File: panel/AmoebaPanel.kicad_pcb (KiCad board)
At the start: 2 copper layers, 92 x 84 mm, 168 parts, among them J1 Conn_01x01_Pin, J2 Conn_01x01_Pin, J3 Conn_01x01_Pin, J4 Conn_01x01_Pin, SW1 SW_SPST

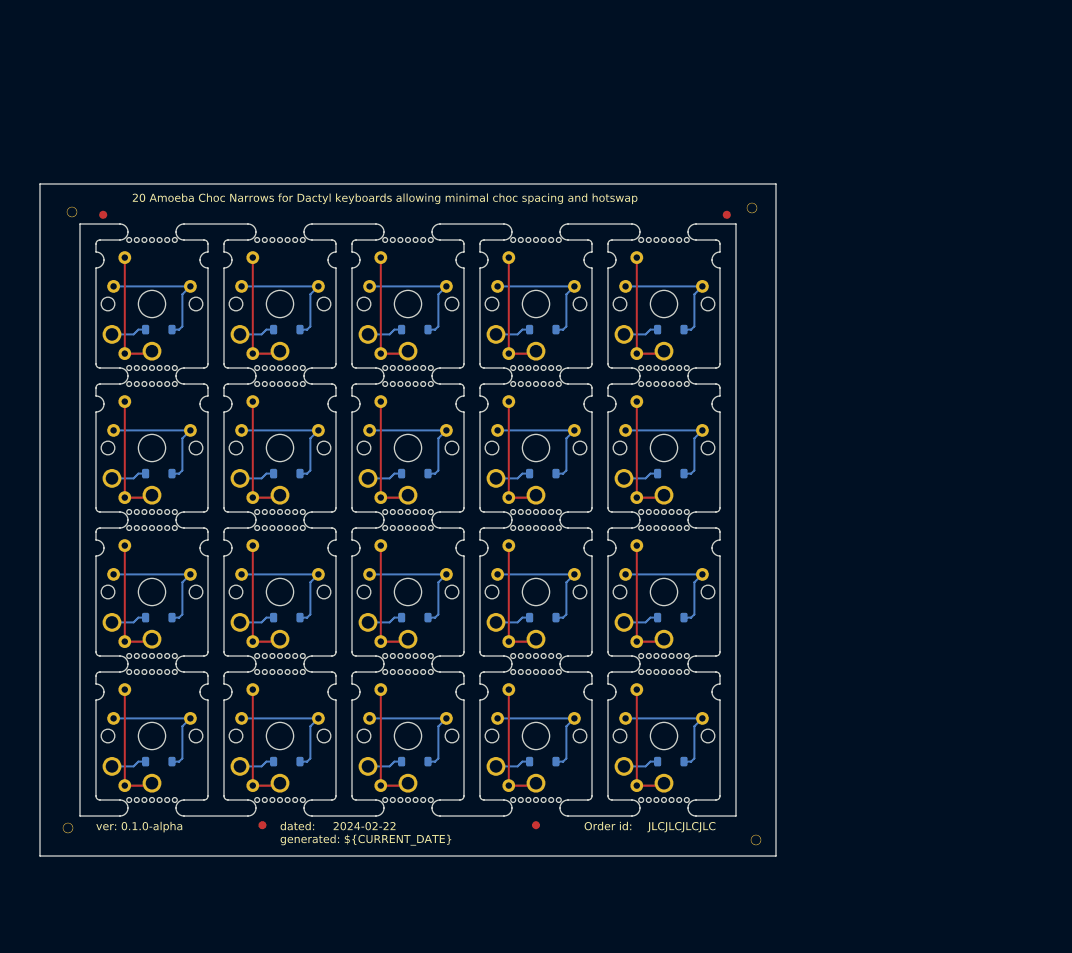
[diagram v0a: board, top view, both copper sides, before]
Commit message: feat(panel): 5 x 5 grid, docs
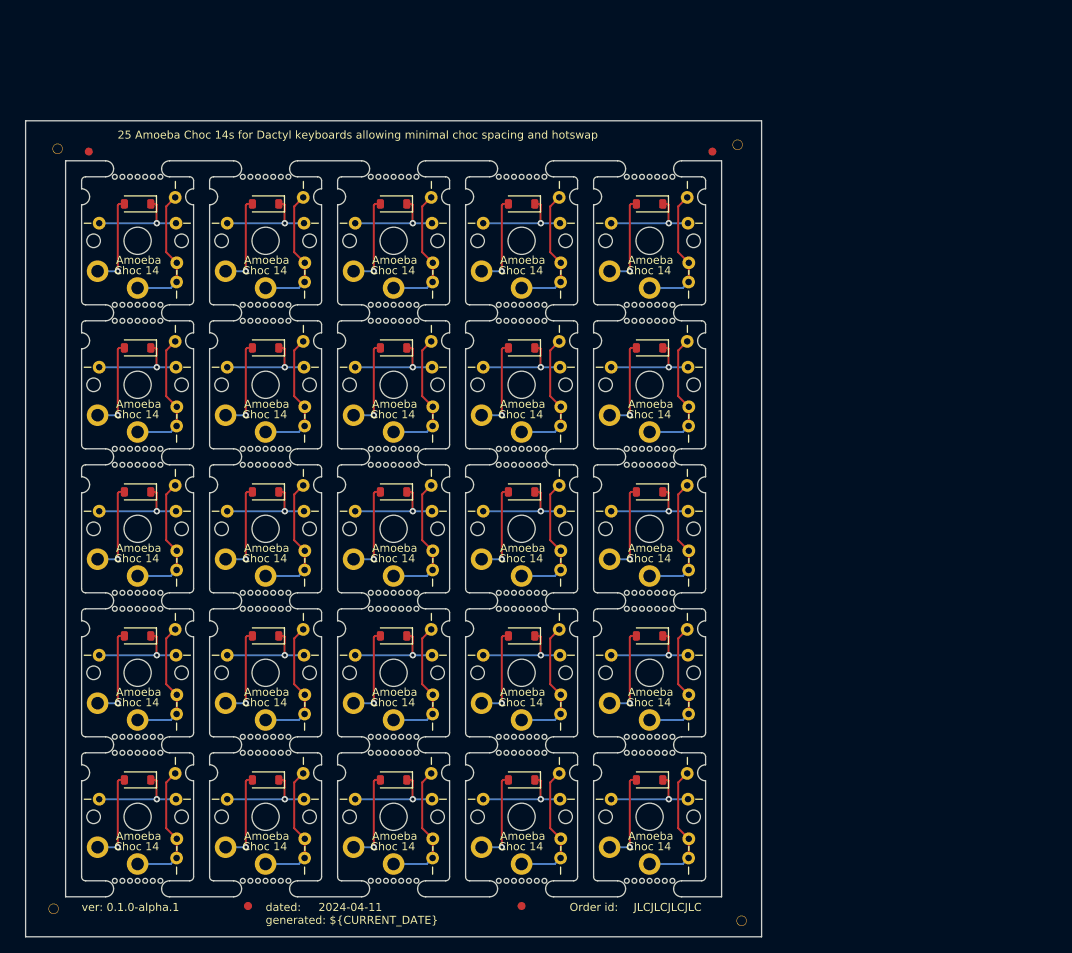
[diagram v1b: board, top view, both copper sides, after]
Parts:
- removed the D1 at (111.8, 107.2)
- removed the D1 at (127.8, 89.2)
- removed the D1 at (175.8, 125.2)
- removed the D1 at (111.8, 89.2)
- removed the D1 at (127.8, 143.2)
- removed the D1 at (127.8, 125.2)
- removed the D1 at (159.8, 107.2)
- removed the D1 at (159.8, 89.2)
- removed the D1 at (111.8, 143.2)
- removed the D1 at (143.8, 89.2)
- removed the D1 at (127.8, 107.2)
- removed the D1 at (143.8, 107.2)
- removed the D1 at (143.8, 143.2)
- removed the D1 at (159.8, 125.2)
- removed the D1 at (175.8, 89.2)
- removed the D1 at (175.8, 143.2)
- removed the D1 at (175.8, 107.2)
- removed the D1 at (111.8, 125.2)
- removed the D1 at (143.8, 125.2)
- removed the D1 at (159.8, 143.2)
- removed the J1 at (107.6, 116.2)
- removed the J1 at (171.6, 134.2)
- removed the J1 at (171.6, 80.2)
- removed the J1 at (139.6, 98.2)
- removed the J1 at (155.6, 134.2)
- removed the J1 at (123.6, 116.2)
- removed the J1 at (107.6, 134.2)
- removed the J1 at (123.6, 134.2)
- removed the J1 at (123.6, 80.2)
- removed the J1 at (171.6, 98.2)
- removed the J1 at (171.6, 116.2)
- removed the J1 at (107.6, 98.2)
- removed the J1 at (123.6, 98.2)
- removed the J1 at (155.6, 98.2)
- removed the J1 at (155.6, 116.2)
- removed the J1 at (139.6, 80.2)
- removed the J1 at (139.6, 116.2)
- removed the J1 at (107.6, 80.2)
- removed the J1 at (139.6, 134.2)
- removed the J1 at (155.6, 80.2)
- removed the J2 at (155.6, 92.2)
- removed the J2 at (123.6, 128.2)
- removed the J2 at (107.6, 128.2)
- removed the J2 at (139.6, 92.2)
- removed the J2 at (139.6, 110.2)
- removed the J2 at (123.6, 110.2)
- removed the J2 at (171.6, 110.2)
- removed the J2 at (107.6, 92.2)
- removed the J2 at (139.6, 128.2)
- removed the J2 at (171.6, 128.2)
- removed the J2 at (155.6, 128.2)
- removed the J2 at (107.6, 146.2)
- removed the J2 at (107.6, 110.2)
- removed the J2 at (123.6, 92.2)
- removed the J2 at (139.6, 146.2)
- removed the J2 at (171.6, 92.2)
- removed the J2 at (155.6, 110.2)
- removed the J2 at (123.6, 146.2)
- removed the J2 at (155.6, 146.2)
- removed the J2 at (171.6, 146.2)
- removed the J3 at (138.2, 119.8)
- removed the J3 at (154.2, 137.8)
- removed the J3 at (106.2, 119.8)
- removed the J3 at (138.2, 101.8)
- removed the J3 at (106.2, 101.8)
- removed the J3 at (106.2, 137.8)
- removed the J3 at (170.2, 83.8)
- removed the J3 at (106.2, 83.8)
- removed the J3 at (154.2, 101.8)
- removed the J3 at (122.2, 83.8)
- removed the J3 at (122.2, 101.8)
- removed the J3 at (154.2, 119.8)
- removed the J3 at (170.2, 101.8)
- removed the J3 at (170.2, 137.8)
- removed the J3 at (138.2, 137.8)
- removed the J3 at (122.2, 137.8)
- removed the J3 at (122.2, 119.8)
- removed the J3 at (138.2, 83.8)
- removed the J3 at (154.2, 83.8)
- removed the J3 at (170.2, 119.8)
- removed the J4 at (131.8, 83.8)
- removed the J4 at (163.8, 119.8)
- removed the J4 at (163.8, 137.8)
- removed the J4 at (131.8, 101.8)
- removed the J4 at (163.8, 83.8)
- removed the J4 at (147.8, 83.8)
- removed the J4 at (147.8, 119.8)
- removed the J4 at (115.8, 83.8)
- removed the J4 at (179.8, 83.8)
- removed the J4 at (179.8, 137.8)
- removed the J4 at (147.8, 137.8)
- removed the J4 at (179.8, 101.8)
- removed the J4 at (115.8, 119.8)
- removed the J4 at (179.8, 119.8)
- removed the J4 at (115.8, 101.8)
- removed the J4 at (131.8, 137.8)
- removed the J4 at (115.8, 137.8)
- removed the J4 at (147.8, 101.8)
- removed the J4 at (131.8, 119.8)
- removed the J4 at (163.8, 101.8)
- removed the REF** at (159.0, 132.0)
- removed the REF** at (175.0, 96.0)
- removed the REF** at (111.0, 114.0)
- removed the REF** at (127.0, 132.0)
- removed the REF** at (175.0, 132.0)
- removed the REF** at (175.0, 112.0)
- removed the REF** at (175.0, 130.0)
- removed the REF** at (175.0, 94.0)
- removed the REF** at (111.0, 96.0)
- removed the REF** at (159.0, 148.0)
- removed the REF** at (127.0, 148.0)
- removed the REF** at (159.0, 78.0)
- removed the REF** at (127.0, 112.0)
- removed the REF** at (143.0, 130.0)
- removed the REF** at (159.0, 96.0)
- removed the REF** at (127.0, 130.0)
- removed the REF** at (111.0, 132.0)
- removed the REF** at (111.0, 78.0)
- removed the REF** at (175.0, 114.0)
- removed the REF** at (143.0, 78.0)
- removed the REF** at (143.0, 94.0)
- removed the REF** at (159.0, 114.0)
- removed the REF** at (127.0, 78.0)
- removed the REF** at (175.0, 78.0)
- removed the REF** at (175.0, 148.0)
- removed the REF** at (143.0, 148.0)
- removed the REF** at (127.0, 94.0)
- removed the REF** at (143.0, 112.0)
- removed the REF** at (111.0, 94.0)
- removed the REF** at (143.0, 114.0)
- removed the REF** at (127.0, 114.0)
- removed the REF** at (143.0, 96.0)
- removed the REF** at (159.0, 112.0)
- removed the REF** at (111.0, 112.0)
- removed the REF** at (159.0, 94.0)
- removed the REF** at (143.0, 132.0)
- removed the REF** at (111.0, 130.0)
- removed the REF** at (111.0, 148.0)
- removed the REF** at (159.0, 130.0)
- removed the REF** at (127.0, 96.0)
- removed the SW1 at (111.0, 122.0)
- removed the SW1 at (159.0, 86.0)
- removed the SW1 at (175.0, 104.0)
- removed the SW1 at (111.0, 86.0)
- removed the SW1 at (111.0, 140.0)
- removed the SW1 at (159.0, 104.0)
- removed the SW1 at (111.0, 104.0)
- removed the SW1 at (175.0, 86.0)
- removed the SW1 at (143.0, 86.0)
- removed the SW1 at (159.0, 140.0)
- removed the SW1 at (143.0, 140.0)
- removed the SW1 at (175.0, 122.0)
- removed the SW1 at (127.0, 122.0)
- removed the SW1 at (127.0, 140.0)
- removed the SW1 at (143.0, 104.0)
- removed the SW1 at (159.0, 122.0)
- removed the SW1 at (127.0, 86.0)
- removed the SW1 at (127.0, 104.0)
- removed the SW1 at (143.0, 122.0)
- removed the SW1 at (175.0, 140.0)
- added D1: 1N4148, Diode_SMD:D_SOD-123, F.Cu at (109.2, 73.5)
- added D10: 1N4148, Diode_SMD:D_SOD-123, F.Cu at (173.2, 91.5)
- added D11: 1N4148, Diode_SMD:D_SOD-123, F.Cu at (109.2, 109.5)
- added D12: 1N4148, Diode_SMD:D_SOD-123, F.Cu at (125.2, 109.5)
- added D13: 1N4148, Diode_SMD:D_SOD-123, F.Cu at (141.2, 109.5)
- added D14: 1N4148, Diode_SMD:D_SOD-123, F.Cu at (157.2, 109.5)
- added D15: 1N4148, Diode_SMD:D_SOD-123, F.Cu at (173.2, 109.5)
- added D16: 1N4148, Diode_SMD:D_SOD-123, F.Cu at (109.2, 127.5)
- added D17: 1N4148, Diode_SMD:D_SOD-123, F.Cu at (125.2, 127.5)
- added D18: 1N4148, Diode_SMD:D_SOD-123, F.Cu at (141.2, 127.5)
- added D19: 1N4148, Diode_SMD:D_SOD-123, F.Cu at (157.2, 127.5)
- added D2: 1N4148, Diode_SMD:D_SOD-123, F.Cu at (125.2, 73.5)
- added D20: 1N4148, Diode_SMD:D_SOD-123, F.Cu at (173.2, 127.5)
- added D21: 1N4148, Diode_SMD:D_SOD-123, F.Cu at (109.2, 145.5)
- added D22: 1N4148, Diode_SMD:D_SOD-123, F.Cu at (125.2, 145.5)
- added D23: 1N4148, Diode_SMD:D_SOD-123, F.Cu at (141.2, 145.5)
- added D24: 1N4148, Diode_SMD:D_SOD-123, F.Cu at (157.2, 145.5)
- added D25: 1N4148, Diode_SMD:D_SOD-123, F.Cu at (173.2, 145.5)
- added D3: 1N4148, Diode_SMD:D_SOD-123, F.Cu at (141.2, 73.5)
- added D4: 1N4148, Diode_SMD:D_SOD-123, F.Cu at (157.2, 73.5)
- added D5: 1N4148, Diode_SMD:D_SOD-123, F.Cu at (173.2, 73.5)
- added D6: 1N4148, Diode_SMD:D_SOD-123, F.Cu at (109.2, 91.5)
- added D7: 1N4148, Diode_SMD:D_SOD-123, F.Cu at (125.2, 91.5)
- added D8: 1N4148, Diode_SMD:D_SOD-123, F.Cu at (141.2, 91.5)
- added D9: 1N4148, Diode_SMD:D_SOD-123, F.Cu at (157.2, 91.5)
- added J1: Conn_01x01_Pin, Amoeba_Choc_Nar:Pin_D0.8mm_L7.0mm, B.Cu at (113.9, 72.7)
- added J10: Conn_01x01_Pin, Amoeba_Choc_Nar:Pin_D0.8mm_L7.0mm, B.Cu at (130.1, 80.8)
- added J100: Conn_01x01_Pin, Amoeba_Choc_Nar:Pin_D0.8mm_L7.0mm, B.Cu at (178.1, 134.8)
- added J101: Conn_01x01_Pin, Amoeba_Choc_Nar:Pin_D0.8mm_L7.0mm, B.Cu at (113.9, 144.7)
- added J102: Conn_01x01_Pin, Amoeba_Choc_Nar:Pin_D0.8mm_L7.0mm, B.Cu at (114.1, 155.2)
- added J103: Conn_01x01_Pin, Amoeba_Choc_Nar:Pin_D0.8mm_L7.0mm, B.Cu at (104.4, 147.9)
- added J104: Conn_01x01_Pin, Amoeba_Choc_Nar:Pin_D0.8mm_L7.0mm, B.Cu at (114.0, 147.9)
- added J105: Conn_01x01_Pin, Amoeba_Choc_Nar:Pin_D0.8mm_L7.0mm, B.Cu at (114.1, 152.8)
- added J106: Conn_01x01_Pin, Amoeba_Choc_Nar:Pin_D0.8mm_L7.0mm, B.Cu at (129.9, 144.7)
- added J107: Conn_01x01_Pin, Amoeba_Choc_Nar:Pin_D0.8mm_L7.0mm, B.Cu at (130.1, 155.2)
- added J108: Conn_01x01_Pin, Amoeba_Choc_Nar:Pin_D0.8mm_L7.0mm, B.Cu at (120.4, 147.9)
- added J109: Conn_01x01_Pin, Amoeba_Choc_Nar:Pin_D0.8mm_L7.0mm, B.Cu at (130.0, 147.9)
- added J11: Conn_01x01_Pin, Amoeba_Choc_Nar:Pin_D0.8mm_L7.0mm, B.Cu at (145.9, 72.7)
- added J110: Conn_01x01_Pin, Amoeba_Choc_Nar:Pin_D0.8mm_L7.0mm, B.Cu at (130.1, 152.8)
- added J111: Conn_01x01_Pin, Amoeba_Choc_Nar:Pin_D0.8mm_L7.0mm, B.Cu at (145.9, 144.7)
- added J112: Conn_01x01_Pin, Amoeba_Choc_Nar:Pin_D0.8mm_L7.0mm, B.Cu at (146.1, 155.2)
- added J113: Conn_01x01_Pin, Amoeba_Choc_Nar:Pin_D0.8mm_L7.0mm, B.Cu at (136.4, 147.9)
- added J114: Conn_01x01_Pin, Amoeba_Choc_Nar:Pin_D0.8mm_L7.0mm, B.Cu at (146.0, 147.9)
- added J115: Conn_01x01_Pin, Amoeba_Choc_Nar:Pin_D0.8mm_L7.0mm, B.Cu at (146.1, 152.8)
- added J116: Conn_01x01_Pin, Amoeba_Choc_Nar:Pin_D0.8mm_L7.0mm, B.Cu at (161.9, 144.7)
- added J117: Conn_01x01_Pin, Amoeba_Choc_Nar:Pin_D0.8mm_L7.0mm, B.Cu at (162.1, 155.2)
- added J118: Conn_01x01_Pin, Amoeba_Choc_Nar:Pin_D0.8mm_L7.0mm, B.Cu at (152.4, 147.9)
- added J119: Conn_01x01_Pin, Amoeba_Choc_Nar:Pin_D0.8mm_L7.0mm, B.Cu at (162.0, 147.9)
- added J12: Conn_01x01_Pin, Amoeba_Choc_Nar:Pin_D0.8mm_L7.0mm, B.Cu at (146.1, 83.2)
- added J120: Conn_01x01_Pin, Amoeba_Choc_Nar:Pin_D0.8mm_L7.0mm, B.Cu at (162.1, 152.8)
- added J121: Conn_01x01_Pin, Amoeba_Choc_Nar:Pin_D0.8mm_L7.0mm, B.Cu at (177.9, 144.7)
- added J122: Conn_01x01_Pin, Amoeba_Choc_Nar:Pin_D0.8mm_L7.0mm, B.Cu at (178.1, 155.2)
- added J123: Conn_01x01_Pin, Amoeba_Choc_Nar:Pin_D0.8mm_L7.0mm, B.Cu at (168.4, 147.9)
- added J124: Conn_01x01_Pin, Amoeba_Choc_Nar:Pin_D0.8mm_L7.0mm, B.Cu at (178.0, 147.9)
- added J125: Conn_01x01_Pin, Amoeba_Choc_Nar:Pin_D0.8mm_L7.0mm, B.Cu at (178.1, 152.8)
- added J13: Conn_01x01_Pin, Amoeba_Choc_Nar:Pin_D0.8mm_L7.0mm, B.Cu at (136.4, 75.9)
- added J14: Conn_01x01_Pin, Amoeba_Choc_Nar:Pin_D0.8mm_L7.0mm, B.Cu at (146.0, 75.9)
- added J15: Conn_01x01_Pin, Amoeba_Choc_Nar:Pin_D0.8mm_L7.0mm, B.Cu at (146.1, 80.8)
- added J16: Conn_01x01_Pin, Amoeba_Choc_Nar:Pin_D0.8mm_L7.0mm, B.Cu at (161.9, 72.7)
- added J17: Conn_01x01_Pin, Amoeba_Choc_Nar:Pin_D0.8mm_L7.0mm, B.Cu at (162.1, 83.2)
- added J18: Conn_01x01_Pin, Amoeba_Choc_Nar:Pin_D0.8mm_L7.0mm, B.Cu at (152.4, 75.9)
- added J19: Conn_01x01_Pin, Amoeba_Choc_Nar:Pin_D0.8mm_L7.0mm, B.Cu at (162.0, 75.9)
- added J2: Conn_01x01_Pin, Amoeba_Choc_Nar:Pin_D0.8mm_L7.0mm, B.Cu at (114.1, 83.2)
- added J20: Conn_01x01_Pin, Amoeba_Choc_Nar:Pin_D0.8mm_L7.0mm, B.Cu at (162.1, 80.8)
- added J21: Conn_01x01_Pin, Amoeba_Choc_Nar:Pin_D0.8mm_L7.0mm, B.Cu at (177.9, 72.7)
- added J22: Conn_01x01_Pin, Amoeba_Choc_Nar:Pin_D0.8mm_L7.0mm, B.Cu at (178.1, 83.2)
- added J23: Conn_01x01_Pin, Amoeba_Choc_Nar:Pin_D0.8mm_L7.0mm, B.Cu at (168.4, 75.9)
- added J24: Conn_01x01_Pin, Amoeba_Choc_Nar:Pin_D0.8mm_L7.0mm, B.Cu at (178.0, 75.9)
- added J25: Conn_01x01_Pin, Amoeba_Choc_Nar:Pin_D0.8mm_L7.0mm, B.Cu at (178.1, 80.8)
- added J26: Conn_01x01_Pin, Amoeba_Choc_Nar:Pin_D0.8mm_L7.0mm, B.Cu at (113.9, 90.7)
- added J27: Conn_01x01_Pin, Amoeba_Choc_Nar:Pin_D0.8mm_L7.0mm, B.Cu at (114.1, 101.2)
- added J28: Conn_01x01_Pin, Amoeba_Choc_Nar:Pin_D0.8mm_L7.0mm, B.Cu at (104.4, 93.9)
- added J29: Conn_01x01_Pin, Amoeba_Choc_Nar:Pin_D0.8mm_L7.0mm, B.Cu at (114.0, 93.9)
- added J3: Conn_01x01_Pin, Amoeba_Choc_Nar:Pin_D0.8mm_L7.0mm, B.Cu at (104.4, 75.9)
- added J30: Conn_01x01_Pin, Amoeba_Choc_Nar:Pin_D0.8mm_L7.0mm, B.Cu at (114.1, 98.8)
- added J31: Conn_01x01_Pin, Amoeba_Choc_Nar:Pin_D0.8mm_L7.0mm, B.Cu at (129.9, 90.7)
- added J32: Conn_01x01_Pin, Amoeba_Choc_Nar:Pin_D0.8mm_L7.0mm, B.Cu at (130.1, 101.2)
- added J33: Conn_01x01_Pin, Amoeba_Choc_Nar:Pin_D0.8mm_L7.0mm, B.Cu at (120.4, 93.9)
- added J34: Conn_01x01_Pin, Amoeba_Choc_Nar:Pin_D0.8mm_L7.0mm, B.Cu at (130.0, 93.9)
- added J35: Conn_01x01_Pin, Amoeba_Choc_Nar:Pin_D0.8mm_L7.0mm, B.Cu at (130.1, 98.8)
- added J36: Conn_01x01_Pin, Amoeba_Choc_Nar:Pin_D0.8mm_L7.0mm, B.Cu at (145.9, 90.7)
- added J37: Conn_01x01_Pin, Amoeba_Choc_Nar:Pin_D0.8mm_L7.0mm, B.Cu at (146.1, 101.2)
- added J38: Conn_01x01_Pin, Amoeba_Choc_Nar:Pin_D0.8mm_L7.0mm, B.Cu at (136.4, 93.9)
- added J39: Conn_01x01_Pin, Amoeba_Choc_Nar:Pin_D0.8mm_L7.0mm, B.Cu at (146.0, 93.9)
- added J4: Conn_01x01_Pin, Amoeba_Choc_Nar:Pin_D0.8mm_L7.0mm, B.Cu at (114.0, 75.9)
- added J40: Conn_01x01_Pin, Amoeba_Choc_Nar:Pin_D0.8mm_L7.0mm, B.Cu at (146.1, 98.8)
- added J41: Conn_01x01_Pin, Amoeba_Choc_Nar:Pin_D0.8mm_L7.0mm, B.Cu at (161.9, 90.7)
- added J42: Conn_01x01_Pin, Amoeba_Choc_Nar:Pin_D0.8mm_L7.0mm, B.Cu at (162.1, 101.2)
- added J43: Conn_01x01_Pin, Amoeba_Choc_Nar:Pin_D0.8mm_L7.0mm, B.Cu at (152.4, 93.9)
- added J44: Conn_01x01_Pin, Amoeba_Choc_Nar:Pin_D0.8mm_L7.0mm, B.Cu at (162.0, 93.9)
- added J45: Conn_01x01_Pin, Amoeba_Choc_Nar:Pin_D0.8mm_L7.0mm, B.Cu at (162.1, 98.8)
- added J46: Conn_01x01_Pin, Amoeba_Choc_Nar:Pin_D0.8mm_L7.0mm, B.Cu at (177.9, 90.7)
- added J47: Conn_01x01_Pin, Amoeba_Choc_Nar:Pin_D0.8mm_L7.0mm, B.Cu at (178.1, 101.2)
- added J48: Conn_01x01_Pin, Amoeba_Choc_Nar:Pin_D0.8mm_L7.0mm, B.Cu at (168.4, 93.9)
- added J49: Conn_01x01_Pin, Amoeba_Choc_Nar:Pin_D0.8mm_L7.0mm, B.Cu at (178.0, 93.9)
- added J5: Conn_01x01_Pin, Amoeba_Choc_Nar:Pin_D0.8mm_L7.0mm, B.Cu at (114.1, 80.8)
- added J50: Conn_01x01_Pin, Amoeba_Choc_Nar:Pin_D0.8mm_L7.0mm, B.Cu at (178.1, 98.8)
- added J51: Conn_01x01_Pin, Amoeba_Choc_Nar:Pin_D0.8mm_L7.0mm, B.Cu at (113.9, 108.7)
- added J52: Conn_01x01_Pin, Amoeba_Choc_Nar:Pin_D0.8mm_L7.0mm, B.Cu at (114.1, 119.2)
- added J53: Conn_01x01_Pin, Amoeba_Choc_Nar:Pin_D0.8mm_L7.0mm, B.Cu at (104.4, 111.9)
- added J54: Conn_01x01_Pin, Amoeba_Choc_Nar:Pin_D0.8mm_L7.0mm, B.Cu at (114.0, 111.9)
- added J55: Conn_01x01_Pin, Amoeba_Choc_Nar:Pin_D0.8mm_L7.0mm, B.Cu at (114.1, 116.8)
- added J56: Conn_01x01_Pin, Amoeba_Choc_Nar:Pin_D0.8mm_L7.0mm, B.Cu at (129.9, 108.7)
- added J57: Conn_01x01_Pin, Amoeba_Choc_Nar:Pin_D0.8mm_L7.0mm, B.Cu at (130.1, 119.2)
- added J58: Conn_01x01_Pin, Amoeba_Choc_Nar:Pin_D0.8mm_L7.0mm, B.Cu at (120.4, 111.9)
- added J59: Conn_01x01_Pin, Amoeba_Choc_Nar:Pin_D0.8mm_L7.0mm, B.Cu at (130.0, 111.9)
- added J6: Conn_01x01_Pin, Amoeba_Choc_Nar:Pin_D0.8mm_L7.0mm, B.Cu at (129.9, 72.7)
- added J60: Conn_01x01_Pin, Amoeba_Choc_Nar:Pin_D0.8mm_L7.0mm, B.Cu at (130.1, 116.8)
- added J61: Conn_01x01_Pin, Amoeba_Choc_Nar:Pin_D0.8mm_L7.0mm, B.Cu at (145.9, 108.7)
- added J62: Conn_01x01_Pin, Amoeba_Choc_Nar:Pin_D0.8mm_L7.0mm, B.Cu at (146.1, 119.2)
- added J63: Conn_01x01_Pin, Amoeba_Choc_Nar:Pin_D0.8mm_L7.0mm, B.Cu at (136.4, 111.9)
- added J64: Conn_01x01_Pin, Amoeba_Choc_Nar:Pin_D0.8mm_L7.0mm, B.Cu at (146.0, 111.9)
- added J65: Conn_01x01_Pin, Amoeba_Choc_Nar:Pin_D0.8mm_L7.0mm, B.Cu at (146.1, 116.8)
- added J66: Conn_01x01_Pin, Amoeba_Choc_Nar:Pin_D0.8mm_L7.0mm, B.Cu at (161.9, 108.7)
- added J67: Conn_01x01_Pin, Amoeba_Choc_Nar:Pin_D0.8mm_L7.0mm, B.Cu at (162.1, 119.2)
- added J68: Conn_01x01_Pin, Amoeba_Choc_Nar:Pin_D0.8mm_L7.0mm, B.Cu at (152.4, 111.9)
- added J69: Conn_01x01_Pin, Amoeba_Choc_Nar:Pin_D0.8mm_L7.0mm, B.Cu at (162.0, 111.9)
- added J7: Conn_01x01_Pin, Amoeba_Choc_Nar:Pin_D0.8mm_L7.0mm, B.Cu at (130.1, 83.2)
- added J70: Conn_01x01_Pin, Amoeba_Choc_Nar:Pin_D0.8mm_L7.0mm, B.Cu at (162.1, 116.8)
- added J71: Conn_01x01_Pin, Amoeba_Choc_Nar:Pin_D0.8mm_L7.0mm, B.Cu at (177.9, 108.7)
- added J72: Conn_01x01_Pin, Amoeba_Choc_Nar:Pin_D0.8mm_L7.0mm, B.Cu at (178.1, 119.2)
- added J73: Conn_01x01_Pin, Amoeba_Choc_Nar:Pin_D0.8mm_L7.0mm, B.Cu at (168.4, 111.9)
- added J74: Conn_01x01_Pin, Amoeba_Choc_Nar:Pin_D0.8mm_L7.0mm, B.Cu at (178.0, 111.9)
- added J75: Conn_01x01_Pin, Amoeba_Choc_Nar:Pin_D0.8mm_L7.0mm, B.Cu at (178.1, 116.8)
- added J76: Conn_01x01_Pin, Amoeba_Choc_Nar:Pin_D0.8mm_L7.0mm, B.Cu at (113.9, 126.7)
- added J77: Conn_01x01_Pin, Amoeba_Choc_Nar:Pin_D0.8mm_L7.0mm, B.Cu at (114.1, 137.2)
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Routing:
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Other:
- board size 92 x 84 mm -> 92 x 102 mm
- board text added: "Amoeba"
- board text added: "Choc 14"

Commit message: feat(panel): update for width 13.7mm
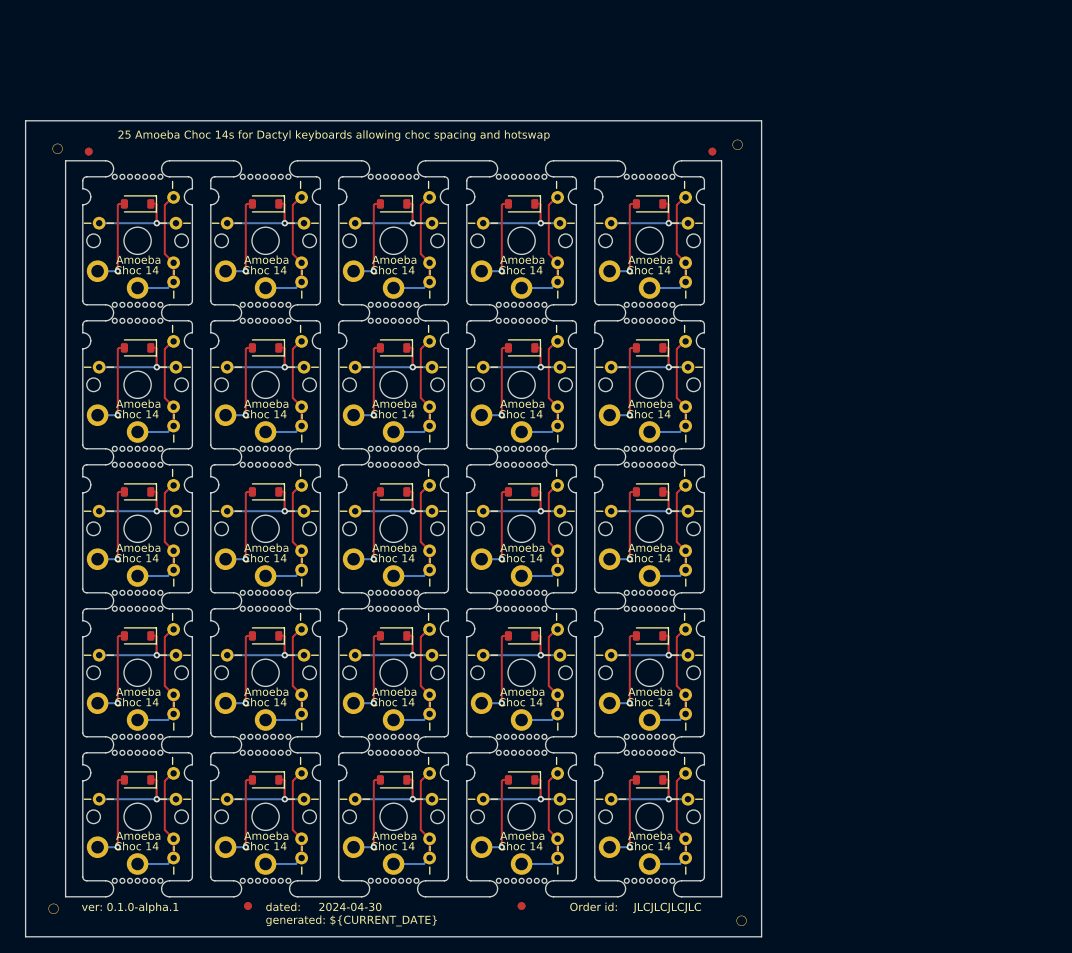
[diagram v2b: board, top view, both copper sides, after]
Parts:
- removed D10, D11, D12, D13, D14, D15, D16, D17, D18, D19, D2, D20, D21, D22, D23, D24, D25, D3, D4, D5, D6, D7, D8, D9: 1N4148, Diode_SMD:D_SOD-123
- removed the J1 at (113.9, 72.7)
- removed J10, J100, J101, J102, J103, J104, J105, J106, J107, J108, J109, J11, J110, J111, J112, J113, J114, J115, J116, J117, J118, J119, J12, J120, J121, J122, J123, J124, J125, J13, J14, J15, J16, J17, J18, J19, J20, J21, J22, J23, J24, J25, J26, J27, J28, J29, J30, J31, J32, J33, J34, J35, J36, J37, J38, J39, J40, J41, J42, J43, J44, J45, J46, J47, J48, J49, J50, J51, J52, J53, J54, J55, J56, J57, J58, J59, J6, J60, J61, J62, J63, J64, J65, J66, J67, J68, J69, J7, J70, J71, J72, J73, J74, J75, J76, J77, J78, J79, J8, J80, J81, J82, J83, J84, J85, J86, J87, J88, J89, J9, J90, J91, J92, J93, J94, J95, J96, J97, J98, J99: Conn_01x01_Pin, Amoeba_Choc_Nar:Pin_D0.8mm_L7.0mm
- removed the J2 at (114.1, 83.2)
- removed the J5 at (114.1, 80.8)
- removed REF**1, REF**10, REF**11, REF**12, REF**13, REF**14, REF**15, REF**16, REF**17, REF**18, REF**19, REF**2, REF**20, REF**21, REF**22, REF**23, REF**24, REF**25, REF**26, REF**27, REF**28, REF**29, REF**3, REF**30, REF**31, REF**32, REF**33, REF**34, REF**35, REF**36, REF**37, REF**38, REF**39, REF**4, REF**40, REF**41, REF**42, REF**43, REF**44, REF**45, REF**46, REF**47, REF**48, REF**5, REF**6, REF**7, REF**8, REF**9: Mouse_Bites, Amoeba_Choc_Nar:Mouse_Bites
- removed SW10, SW11, SW12, SW13, SW14, SW15, SW16, SW17, SW18, SW19, SW2, SW20, SW21, SW22, SW23, SW24, SW25, SW3, SW4, SW5, SW6, SW7, SW8, SW9: SW_SPST, Amoeba_Choc_Nar:pg1350-hotswap
- added D1: 1N4148, Diode_SMD:D_SOD-123, F.Cu at (109.2, 127.5)
- added D1: 1N4148, Diode_SMD:D_SOD-123, F.Cu at (125.2, 73.5)
- added D1: 1N4148, Diode_SMD:D_SOD-123, F.Cu at (109.2, 91.5)
- added D1: 1N4148, Diode_SMD:D_SOD-123, F.Cu at (125.2, 109.5)
- added D1: 1N4148, Diode_SMD:D_SOD-123, F.Cu at (125.2, 145.5)
- added D1: 1N4148, Diode_SMD:D_SOD-123, F.Cu at (157.2, 73.5)
- added D1: 1N4148, Diode_SMD:D_SOD-123, F.Cu at (141.2, 73.5)
- added D1: 1N4148, Diode_SMD:D_SOD-123, F.Cu at (173.2, 127.5)
- added D1: 1N4148, Diode_SMD:D_SOD-123, F.Cu at (109.2, 145.5)
- added D1: 1N4148, Diode_SMD:D_SOD-123, F.Cu at (141.2, 91.5)
- added D1: 1N4148, Diode_SMD:D_SOD-123, F.Cu at (141.2, 127.5)
- added D1: 1N4148, Diode_SMD:D_SOD-123, F.Cu at (141.2, 109.5)
- added D1: 1N4148, Diode_SMD:D_SOD-123, F.Cu at (157.2, 145.5)
- added D1: 1N4148, Diode_SMD:D_SOD-123, F.Cu at (173.2, 109.5)
- added D1: 1N4148, Diode_SMD:D_SOD-123, F.Cu at (109.2, 109.5)
- added D1: 1N4148, Diode_SMD:D_SOD-123, F.Cu at (157.2, 91.5)
- added D1: 1N4148, Diode_SMD:D_SOD-123, F.Cu at (173.2, 73.5)
- added D1: 1N4148, Diode_SMD:D_SOD-123, F.Cu at (125.2, 91.5)
- added D1: 1N4148, Diode_SMD:D_SOD-123, F.Cu at (125.2, 127.5)
- added D1: 1N4148, Diode_SMD:D_SOD-123, F.Cu at (141.2, 145.5)
- added D1: 1N4148, Diode_SMD:D_SOD-123, F.Cu at (157.2, 109.5)
- added D1: 1N4148, Diode_SMD:D_SOD-123, F.Cu at (173.2, 145.5)
- added D1: 1N4148, Diode_SMD:D_SOD-123, F.Cu at (173.2, 91.5)
- added D1: 1N4148, Diode_SMD:D_SOD-123, F.Cu at (157.2, 127.5)
- added J1: Conn_01x01_Pin, Amoeba_Choc_Nar:Pin_D0.8mm_L7.0mm, B.Cu at (145.7, 90.7)
- added J1: Conn_01x01_Pin, Amoeba_Choc_Nar:Pin_D0.8mm_L7.0mm, B.Cu at (113.7, 108.7)
- added J1: Conn_01x01_Pin, Amoeba_Choc_Nar:Pin_D0.8mm_L7.0mm, B.Cu at (177.7, 126.7)
- added J1: Conn_01x01_Pin, Amoeba_Choc_Nar:Pin_D0.8mm_L7.0mm, B.Cu at (161.7, 90.7)
- added J1: Conn_01x01_Pin, Amoeba_Choc_Nar:Pin_D0.8mm_L7.0mm, B.Cu at (145.7, 72.7)
- added J1: Conn_01x01_Pin, Amoeba_Choc_Nar:Pin_D0.8mm_L7.0mm, B.Cu at (161.7, 72.7)
- added J1: Conn_01x01_Pin, Amoeba_Choc_Nar:Pin_D0.8mm_L7.0mm, B.Cu at (129.7, 72.7)
- added J1: Conn_01x01_Pin, Amoeba_Choc_Nar:Pin_D0.8mm_L7.0mm, B.Cu at (145.7, 126.7)
- added J1: Conn_01x01_Pin, Amoeba_Choc_Nar:Pin_D0.8mm_L7.0mm, B.Cu at (129.7, 144.7)
- added J1: Conn_01x01_Pin, Amoeba_Choc_Nar:Pin_D0.8mm_L7.0mm, B.Cu at (129.7, 90.7)
- added J1: Conn_01x01_Pin, Amoeba_Choc_Nar:Pin_D0.8mm_L7.0mm, B.Cu at (145.7, 144.7)
- added J1: Conn_01x01_Pin, Amoeba_Choc_Nar:Pin_D0.8mm_L7.0mm, B.Cu at (161.7, 108.7)
- added J1: Conn_01x01_Pin, Amoeba_Choc_Nar:Pin_D0.8mm_L7.0mm, B.Cu at (177.7, 90.7)
- added J1: Conn_01x01_Pin, Amoeba_Choc_Nar:Pin_D0.8mm_L7.0mm, B.Cu at (177.7, 72.7)
- added J1: Conn_01x01_Pin, Amoeba_Choc_Nar:Pin_D0.8mm_L7.0mm, B.Cu at (113.7, 126.7)
- added J1: Conn_01x01_Pin, Amoeba_Choc_Nar:Pin_D0.8mm_L7.0mm, B.Cu at (113.7, 144.7)
- added J1: Conn_01x01_Pin, Amoeba_Choc_Nar:Pin_D0.8mm_L7.0mm, B.Cu at (113.7, 90.7)
- added J1: Conn_01x01_Pin, Amoeba_Choc_Nar:Pin_D0.8mm_L7.0mm, B.Cu at (177.7, 108.7)
- added J1: Conn_01x01_Pin, Amoeba_Choc_Nar:Pin_D0.8mm_L7.0mm, B.Cu at (161.7, 144.7)
- added J1: Conn_01x01_Pin, Amoeba_Choc_Nar:Pin_D0.8mm_L7.0mm, B.Cu at (113.7, 72.7)
- added J1: Conn_01x01_Pin, Amoeba_Choc_Nar:Pin_D0.8mm_L7.0mm, B.Cu at (129.7, 126.7)
- added J1: Conn_01x01_Pin, Amoeba_Choc_Nar:Pin_D0.8mm_L7.0mm, B.Cu at (145.7, 108.7)
- added J1: Conn_01x01_Pin, Amoeba_Choc_Nar:Pin_D0.8mm_L7.0mm, B.Cu at (177.7, 144.7)
- added J1: Conn_01x01_Pin, Amoeba_Choc_Nar:Pin_D0.8mm_L7.0mm, B.Cu at (161.7, 126.7)
- added J1: Conn_01x01_Pin, Amoeba_Choc_Nar:Pin_D0.8mm_L7.0mm, B.Cu at (129.7, 108.7)
- added J2: Conn_01x01_Pin, Amoeba_Choc_Nar:Pin_D0.8mm_L7.0mm, B.Cu at (161.7, 83.2)
- added J2: Conn_01x01_Pin, Amoeba_Choc_Nar:Pin_D0.8mm_L7.0mm, B.Cu at (177.7, 101.2)
- added J2: Conn_01x01_Pin, Amoeba_Choc_Nar:Pin_D0.8mm_L7.0mm, B.Cu at (161.7, 101.2)
- added J2: Conn_01x01_Pin, Amoeba_Choc_Nar:Pin_D0.8mm_L7.0mm, B.Cu at (129.7, 155.2)
- added J2: Conn_01x01_Pin, Amoeba_Choc_Nar:Pin_D0.8mm_L7.0mm, B.Cu at (177.7, 119.2)
- added J2: Conn_01x01_Pin, Amoeba_Choc_Nar:Pin_D0.8mm_L7.0mm, B.Cu at (129.7, 119.2)
- added J2: Conn_01x01_Pin, Amoeba_Choc_Nar:Pin_D0.8mm_L7.0mm, B.Cu at (145.7, 83.2)
- added J2: Conn_01x01_Pin, Amoeba_Choc_Nar:Pin_D0.8mm_L7.0mm, B.Cu at (129.7, 83.2)
- added J2: Conn_01x01_Pin, Amoeba_Choc_Nar:Pin_D0.8mm_L7.0mm, B.Cu at (177.7, 83.2)
- added J2: Conn_01x01_Pin, Amoeba_Choc_Nar:Pin_D0.8mm_L7.0mm, B.Cu at (129.7, 101.2)
- added J2: Conn_01x01_Pin, Amoeba_Choc_Nar:Pin_D0.8mm_L7.0mm, B.Cu at (145.7, 101.2)
- added J2: Conn_01x01_Pin, Amoeba_Choc_Nar:Pin_D0.8mm_L7.0mm, B.Cu at (113.7, 119.2)
- added J2: Conn_01x01_Pin, Amoeba_Choc_Nar:Pin_D0.8mm_L7.0mm, B.Cu at (113.7, 101.2)
- added J2: Conn_01x01_Pin, Amoeba_Choc_Nar:Pin_D0.8mm_L7.0mm, B.Cu at (161.7, 119.2)
- added J2: Conn_01x01_Pin, Amoeba_Choc_Nar:Pin_D0.8mm_L7.0mm, B.Cu at (177.7, 137.2)
- added J2: Conn_01x01_Pin, Amoeba_Choc_Nar:Pin_D0.8mm_L7.0mm, B.Cu at (145.7, 137.2)
- added J2: Conn_01x01_Pin, Amoeba_Choc_Nar:Pin_D0.8mm_L7.0mm, B.Cu at (145.7, 119.2)
- added J2: Conn_01x01_Pin, Amoeba_Choc_Nar:Pin_D0.8mm_L7.0mm, B.Cu at (161.7, 137.2)
- added J2: Conn_01x01_Pin, Amoeba_Choc_Nar:Pin_D0.8mm_L7.0mm, B.Cu at (161.7, 155.2)
- added J2: Conn_01x01_Pin, Amoeba_Choc_Nar:Pin_D0.8mm_L7.0mm, B.Cu at (113.7, 83.2)
- added J2: Conn_01x01_Pin, Amoeba_Choc_Nar:Pin_D0.8mm_L7.0mm, B.Cu at (145.7, 155.2)
- added J2: Conn_01x01_Pin, Amoeba_Choc_Nar:Pin_D0.8mm_L7.0mm, B.Cu at (113.7, 155.2)
- added J2: Conn_01x01_Pin, Amoeba_Choc_Nar:Pin_D0.8mm_L7.0mm, B.Cu at (129.7, 137.2)
- added J2: Conn_01x01_Pin, Amoeba_Choc_Nar:Pin_D0.8mm_L7.0mm, B.Cu at (113.7, 137.2)
- added J2: Conn_01x01_Pin, Amoeba_Choc_Nar:Pin_D0.8mm_L7.0mm, B.Cu at (177.7, 155.2)
- added J3: Conn_01x01_Pin, Amoeba_Choc_Nar:Pin_D0.8mm_L7.0mm, B.Cu at (136.4, 129.9)
- added J3: Conn_01x01_Pin, Amoeba_Choc_Nar:Pin_D0.8mm_L7.0mm, B.Cu at (120.4, 75.9)
- added J3: Conn_01x01_Pin, Amoeba_Choc_Nar:Pin_D0.8mm_L7.0mm, B.Cu at (104.4, 129.9)
- added J3: Conn_01x01_Pin, Amoeba_Choc_Nar:Pin_D0.8mm_L7.0mm, B.Cu at (104.4, 111.9)
- added J3: Conn_01x01_Pin, Amoeba_Choc_Nar:Pin_D0.8mm_L7.0mm, B.Cu at (136.4, 111.9)
- added J3: Conn_01x01_Pin, Amoeba_Choc_Nar:Pin_D0.8mm_L7.0mm, B.Cu at (104.4, 93.9)
- added J3: Conn_01x01_Pin, Amoeba_Choc_Nar:Pin_D0.8mm_L7.0mm, B.Cu at (104.4, 147.9)
- added J3: Conn_01x01_Pin, Amoeba_Choc_Nar:Pin_D0.8mm_L7.0mm, B.Cu at (168.4, 75.9)
- added J3: Conn_01x01_Pin, Amoeba_Choc_Nar:Pin_D0.8mm_L7.0mm, B.Cu at (168.4, 147.9)
- added J3: Conn_01x01_Pin, Amoeba_Choc_Nar:Pin_D0.8mm_L7.0mm, B.Cu at (120.4, 129.9)
- added J3: Conn_01x01_Pin, Amoeba_Choc_Nar:Pin_D0.8mm_L7.0mm, B.Cu at (120.4, 147.9)
- added J3: Conn_01x01_Pin, Amoeba_Choc_Nar:Pin_D0.8mm_L7.0mm, B.Cu at (136.4, 93.9)
- added J3: Conn_01x01_Pin, Amoeba_Choc_Nar:Pin_D0.8mm_L7.0mm, B.Cu at (168.4, 129.9)
- added J3: Conn_01x01_Pin, Amoeba_Choc_Nar:Pin_D0.8mm_L7.0mm, B.Cu at (136.4, 75.9)
- added J3: Conn_01x01_Pin, Amoeba_Choc_Nar:Pin_D0.8mm_L7.0mm, B.Cu at (152.4, 93.9)
- added J3: Conn_01x01_Pin, Amoeba_Choc_Nar:Pin_D0.8mm_L7.0mm, B.Cu at (120.4, 111.9)
- added J3: Conn_01x01_Pin, Amoeba_Choc_Nar:Pin_D0.8mm_L7.0mm, B.Cu at (152.4, 111.9)
- added J3: Conn_01x01_Pin, Amoeba_Choc_Nar:Pin_D0.8mm_L7.0mm, B.Cu at (136.4, 147.9)
- added J3: Conn_01x01_Pin, Amoeba_Choc_Nar:Pin_D0.8mm_L7.0mm, B.Cu at (120.4, 93.9)
- added J3: Conn_01x01_Pin, Amoeba_Choc_Nar:Pin_D0.8mm_L7.0mm, B.Cu at (152.4, 147.9)
- added J3: Conn_01x01_Pin, Amoeba_Choc_Nar:Pin_D0.8mm_L7.0mm, B.Cu at (152.4, 75.9)
- added J3: Conn_01x01_Pin, Amoeba_Choc_Nar:Pin_D0.8mm_L7.0mm, B.Cu at (152.4, 129.9)
- added J3: Conn_01x01_Pin, Amoeba_Choc_Nar:Pin_D0.8mm_L7.0mm, B.Cu at (168.4, 93.9)
- added J3: Conn_01x01_Pin, Amoeba_Choc_Nar:Pin_D0.8mm_L7.0mm, B.Cu at (168.4, 111.9)
- added J4: Conn_01x01_Pin, Amoeba_Choc_Nar:Pin_D0.8mm_L7.0mm, B.Cu at (114.0, 147.9)
- added J4: Conn_01x01_Pin, Amoeba_Choc_Nar:Pin_D0.8mm_L7.0mm, B.Cu at (178.0, 111.9)
- added J4: Conn_01x01_Pin, Amoeba_Choc_Nar:Pin_D0.8mm_L7.0mm, B.Cu at (178.0, 93.9)
- added J4: Conn_01x01_Pin, Amoeba_Choc_Nar:Pin_D0.8mm_L7.0mm, B.Cu at (130.0, 75.9)
- added J4: Conn_01x01_Pin, Amoeba_Choc_Nar:Pin_D0.8mm_L7.0mm, B.Cu at (146.0, 75.9)
- added J4: Conn_01x01_Pin, Amoeba_Choc_Nar:Pin_D0.8mm_L7.0mm, B.Cu at (178.0, 147.9)
- added J4: Conn_01x01_Pin, Amoeba_Choc_Nar:Pin_D0.8mm_L7.0mm, B.Cu at (130.0, 93.9)
- added J4: Conn_01x01_Pin, Amoeba_Choc_Nar:Pin_D0.8mm_L7.0mm, B.Cu at (162.0, 129.9)
- added J4: Conn_01x01_Pin, Amoeba_Choc_Nar:Pin_D0.8mm_L7.0mm, B.Cu at (146.0, 147.9)
- added J4: Conn_01x01_Pin, Amoeba_Choc_Nar:Pin_D0.8mm_L7.0mm, B.Cu at (130.0, 111.9)
- added J4: Conn_01x01_Pin, Amoeba_Choc_Nar:Pin_D0.8mm_L7.0mm, B.Cu at (130.0, 147.9)
- added J4: Conn_01x01_Pin, Amoeba_Choc_Nar:Pin_D0.8mm_L7.0mm, B.Cu at (146.0, 129.9)
- added J4: Conn_01x01_Pin, Amoeba_Choc_Nar:Pin_D0.8mm_L7.0mm, B.Cu at (178.0, 75.9)
- added J4: Conn_01x01_Pin, Amoeba_Choc_Nar:Pin_D0.8mm_L7.0mm, B.Cu at (146.0, 111.9)
- added J4: Conn_01x01_Pin, Amoeba_Choc_Nar:Pin_D0.8mm_L7.0mm, B.Cu at (146.0, 93.9)
- added J4: Conn_01x01_Pin, Amoeba_Choc_Nar:Pin_D0.8mm_L7.0mm, B.Cu at (114.0, 93.9)
- added J4: Conn_01x01_Pin, Amoeba_Choc_Nar:Pin_D0.8mm_L7.0mm, B.Cu at (162.0, 93.9)
- added J4: Conn_01x01_Pin, Amoeba_Choc_Nar:Pin_D0.8mm_L7.0mm, B.Cu at (162.0, 111.9)
- added J4: Conn_01x01_Pin, Amoeba_Choc_Nar:Pin_D0.8mm_L7.0mm, B.Cu at (162.0, 75.9)
- added J4: Conn_01x01_Pin, Amoeba_Choc_Nar:Pin_D0.8mm_L7.0mm, B.Cu at (162.0, 147.9)
- added J4: Conn_01x01_Pin, Amoeba_Choc_Nar:Pin_D0.8mm_L7.0mm, B.Cu at (130.0, 129.9)
- added J4: Conn_01x01_Pin, Amoeba_Choc_Nar:Pin_D0.8mm_L7.0mm, B.Cu at (114.0, 111.9)
- added J4: Conn_01x01_Pin, Amoeba_Choc_Nar:Pin_D0.8mm_L7.0mm, B.Cu at (178.0, 129.9)
- added J4: Conn_01x01_Pin, Amoeba_Choc_Nar:Pin_D0.8mm_L7.0mm, B.Cu at (114.0, 129.9)
- added J5: Conn_01x01_Pin, Amoeba_Choc_Nar:Pin_D0.8mm_L7.0mm, B.Cu at (145.7, 134.8)
- added J5: Conn_01x01_Pin, Amoeba_Choc_Nar:Pin_D0.8mm_L7.0mm, B.Cu at (113.7, 98.8)
- added J5: Conn_01x01_Pin, Amoeba_Choc_Nar:Pin_D0.8mm_L7.0mm, B.Cu at (145.7, 98.8)
- added J5: Conn_01x01_Pin, Amoeba_Choc_Nar:Pin_D0.8mm_L7.0mm, B.Cu at (113.7, 152.8)
- added J5: Conn_01x01_Pin, Amoeba_Choc_Nar:Pin_D0.8mm_L7.0mm, B.Cu at (161.7, 134.8)
- added J5: Conn_01x01_Pin, Amoeba_Choc_Nar:Pin_D0.8mm_L7.0mm, B.Cu at (129.7, 152.8)
- added J5: Conn_01x01_Pin, Amoeba_Choc_Nar:Pin_D0.8mm_L7.0mm, B.Cu at (177.7, 98.8)
- added J5: Conn_01x01_Pin, Amoeba_Choc_Nar:Pin_D0.8mm_L7.0mm, B.Cu at (145.7, 80.8)
- added J5: Conn_01x01_Pin, Amoeba_Choc_Nar:Pin_D0.8mm_L7.0mm, B.Cu at (177.7, 152.8)
- added J5: Conn_01x01_Pin, Amoeba_Choc_Nar:Pin_D0.8mm_L7.0mm, B.Cu at (129.7, 98.8)
- added J5: Conn_01x01_Pin, Amoeba_Choc_Nar:Pin_D0.8mm_L7.0mm, B.Cu at (129.7, 134.8)
- added J5: Conn_01x01_Pin, Amoeba_Choc_Nar:Pin_D0.8mm_L7.0mm, B.Cu at (161.7, 80.8)
- added J5: Conn_01x01_Pin, Amoeba_Choc_Nar:Pin_D0.8mm_L7.0mm, B.Cu at (177.7, 134.8)
- added J5: Conn_01x01_Pin, Amoeba_Choc_Nar:Pin_D0.8mm_L7.0mm, B.Cu at (177.7, 116.8)
- added J5: Conn_01x01_Pin, Amoeba_Choc_Nar:Pin_D0.8mm_L7.0mm, B.Cu at (129.7, 80.8)
- added J5: Conn_01x01_Pin, Amoeba_Choc_Nar:Pin_D0.8mm_L7.0mm, B.Cu at (161.7, 98.8)
- added J5: Conn_01x01_Pin, Amoeba_Choc_Nar:Pin_D0.8mm_L7.0mm, B.Cu at (113.7, 80.8)
- added J5: Conn_01x01_Pin, Amoeba_Choc_Nar:Pin_D0.8mm_L7.0mm, B.Cu at (145.7, 116.8)
- added J5: Conn_01x01_Pin, Amoeba_Choc_Nar:Pin_D0.8mm_L7.0mm, B.Cu at (129.7, 116.8)
- added J5: Conn_01x01_Pin, Amoeba_Choc_Nar:Pin_D0.8mm_L7.0mm, B.Cu at (113.7, 116.8)
- added J5: Conn_01x01_Pin, Amoeba_Choc_Nar:Pin_D0.8mm_L7.0mm, B.Cu at (161.7, 116.8)
- added J5: Conn_01x01_Pin, Amoeba_Choc_Nar:Pin_D0.8mm_L7.0mm, B.Cu at (177.7, 80.8)
- added J5: Conn_01x01_Pin, Amoeba_Choc_Nar:Pin_D0.8mm_L7.0mm, B.Cu at (113.7, 134.8)
- added J5: Conn_01x01_Pin, Amoeba_Choc_Nar:Pin_D0.8mm_L7.0mm, B.Cu at (145.7, 152.8)
- added J5: Conn_01x01_Pin, Amoeba_Choc_Nar:Pin_D0.8mm_L7.0mm, B.Cu at (161.7, 152.8)
- added REF**: Mouse_Bites, Amoeba_Choc_Nar:Mouse_Bites, F.Cu at (157.2, 106.1)
- added REF**: Mouse_Bites, Amoeba_Choc_Nar:Mouse_Bites, F.Cu at (173.2, 124.1)
- added REF**: Mouse_Bites, Amoeba_Choc_Nar:Mouse_Bites, F.Cu at (109.2, 104.1)
- added REF**: Mouse_Bites, Amoeba_Choc_Nar:Mouse_Bites, F.Cu at (157.2, 70.1)
- added REF**: Mouse_Bites, Amoeba_Choc_Nar:Mouse_Bites, F.Cu at (109.2, 122.1)
- added REF**: Mouse_Bites, Amoeba_Choc_Nar:Mouse_Bites, F.Cu at (157.2, 122.1)
- added REF**: Mouse_Bites, Amoeba_Choc_Nar:Mouse_Bites, F.Cu at (109.2, 158.1)
- added REF**: Mouse_Bites, Amoeba_Choc_Nar:Mouse_Bites, F.Cu at (125.2, 122.1)
- added REF**: Mouse_Bites, Amoeba_Choc_Nar:Mouse_Bites, F.Cu at (125.2, 104.1)
- added REF**: Mouse_Bites, Amoeba_Choc_Nar:Mouse_Bites, F.Cu at (141.2, 140.1)
- added REF**: Mouse_Bites, Amoeba_Choc_Nar:Mouse_Bites, F.Cu at (157.2, 88.1)
- added REF**: Mouse_Bites, Amoeba_Choc_Nar:Mouse_Bites, F.Cu at (109.2, 124.1)
- added REF**: Mouse_Bites, Amoeba_Choc_Nar:Mouse_Bites, F.Cu at (157.2, 124.1)
- added REF**: Mouse_Bites, Amoeba_Choc_Nar:Mouse_Bites, F.Cu at (173.2, 158.1)
- added REF**: Mouse_Bites, Amoeba_Choc_Nar:Mouse_Bites, F.Cu at (141.2, 88.1)
- added REF**: Mouse_Bites, Amoeba_Choc_Nar:Mouse_Bites, F.Cu at (141.2, 104.1)
- added REF**: Mouse_Bites, Amoeba_Choc_Nar:Mouse_Bites, F.Cu at (141.2, 106.1)
- added REF**: Mouse_Bites, Amoeba_Choc_Nar:Mouse_Bites, F.Cu at (141.2, 70.1)
- added REF**: Mouse_Bites, Amoeba_Choc_Nar:Mouse_Bites, F.Cu at (125.2, 140.1)
- added REF**: Mouse_Bites, Amoeba_Choc_Nar:Mouse_Bites, F.Cu at (173.2, 104.1)
- added REF**: Mouse_Bites, Amoeba_Choc_Nar:Mouse_Bites, F.Cu at (125.2, 86.1)
- added REF**: Mouse_Bites, Amoeba_Choc_Nar:Mouse_Bites, F.Cu at (173.2, 122.1)
- added REF**: Mouse_Bites, Amoeba_Choc_Nar:Mouse_Bites, F.Cu at (109.2, 142.1)
- added REF**: Mouse_Bites, Amoeba_Choc_Nar:Mouse_Bites, F.Cu at (157.2, 140.1)
- added REF**: Mouse_Bites, Amoeba_Choc_Nar:Mouse_Bites, F.Cu at (157.2, 104.1)
- added REF**: Mouse_Bites, Amoeba_Choc_Nar:Mouse_Bites, F.Cu at (141.2, 122.1)
- added REF**: Mouse_Bites, Amoeba_Choc_Nar:Mouse_Bites, F.Cu at (125.2, 124.1)
- added REF**: Mouse_Bites, Amoeba_Choc_Nar:Mouse_Bites, F.Cu at (173.2, 86.1)
- added REF**: Mouse_Bites, Amoeba_Choc_Nar:Mouse_Bites, F.Cu at (109.2, 106.1)
- added REF**: Mouse_Bites, Amoeba_Choc_Nar:Mouse_Bites, F.Cu at (141.2, 158.1)
- added REF**: Mouse_Bites, Amoeba_Choc_Nar:Mouse_Bites, F.Cu at (125.2, 106.1)
- added REF**: Mouse_Bites, Amoeba_Choc_Nar:Mouse_Bites, F.Cu at (173.2, 70.1)
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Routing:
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
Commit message: feat(panel): mouse bites on rails, fix lib path
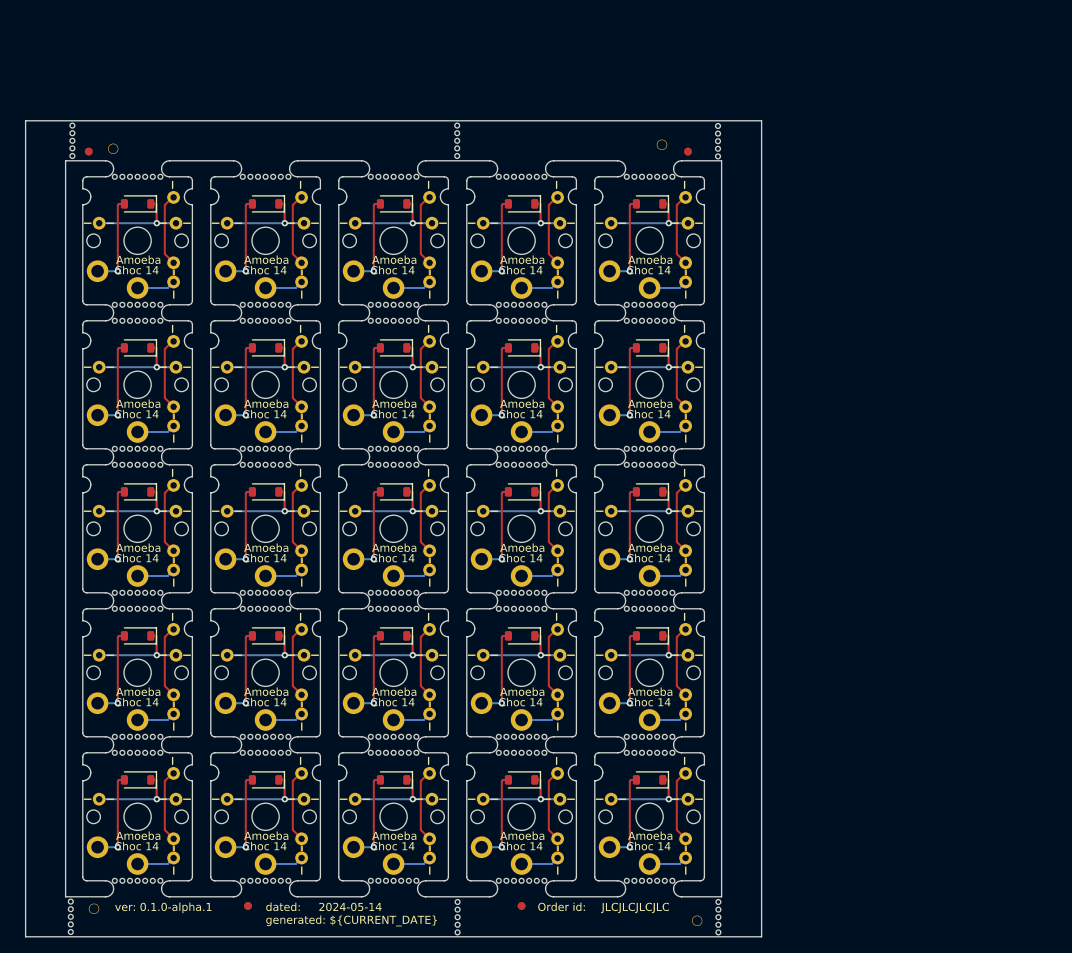
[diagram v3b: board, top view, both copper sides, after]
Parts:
- added REF**: Mouse_Bites_5mm, Amoeba_Choc_Nar:Mouse_Bites_5mm, F.Cu at (181.8, 162.7)
- added REF**: Mouse_Bites_5mm, Amoeba_Choc_Nar:Mouse_Bites_5mm, F.Cu at (181.8, 65.7)
- added REF**: Mouse_Bites_5mm, Amoeba_Choc_Nar:Mouse_Bites_5mm, F.Cu at (100.8, 162.6)
- added REF**: Mouse_Bites_5mm, Amoeba_Choc_Nar:Mouse_Bites_5mm, F.Cu at (149.2, 65.6)
- added REF**: Mouse_Bites_5mm, Amoeba_Choc_Nar:Mouse_Bites_5mm, F.Cu at (101.0, 65.6)
- added REF**: Mouse_Bites_5mm, Amoeba_Choc_Nar:Mouse_Bites_5mm, F.Cu at (149.2, 162.7)
- moved ? 9.45 mm to (174.8, 66.1)
- moved ? 6.95 mm to (106.2, 66.6)
- moved ? 5.55 mm to (179.2, 163.1)
- moved ? 5.05 mm to (103.8, 161.6)
- moved REF** 3.05 mm to (178.0, 67.0)
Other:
- board text removed: "${COMMENT4}"
